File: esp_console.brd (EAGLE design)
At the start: 121.9 x 81.9 mm, 37 parts, among them IC1 74AHC1G04DBV, IC2 UA78M05DCY, J2 10118193-0001LF, Q1 12mhz, Q2 ON_SEMICONDUCTOR_BC849BLT1GON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, Q3 ON_SEMICONDUCTOR_BC849BLT1GON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, SW1 OS102011MA1Q

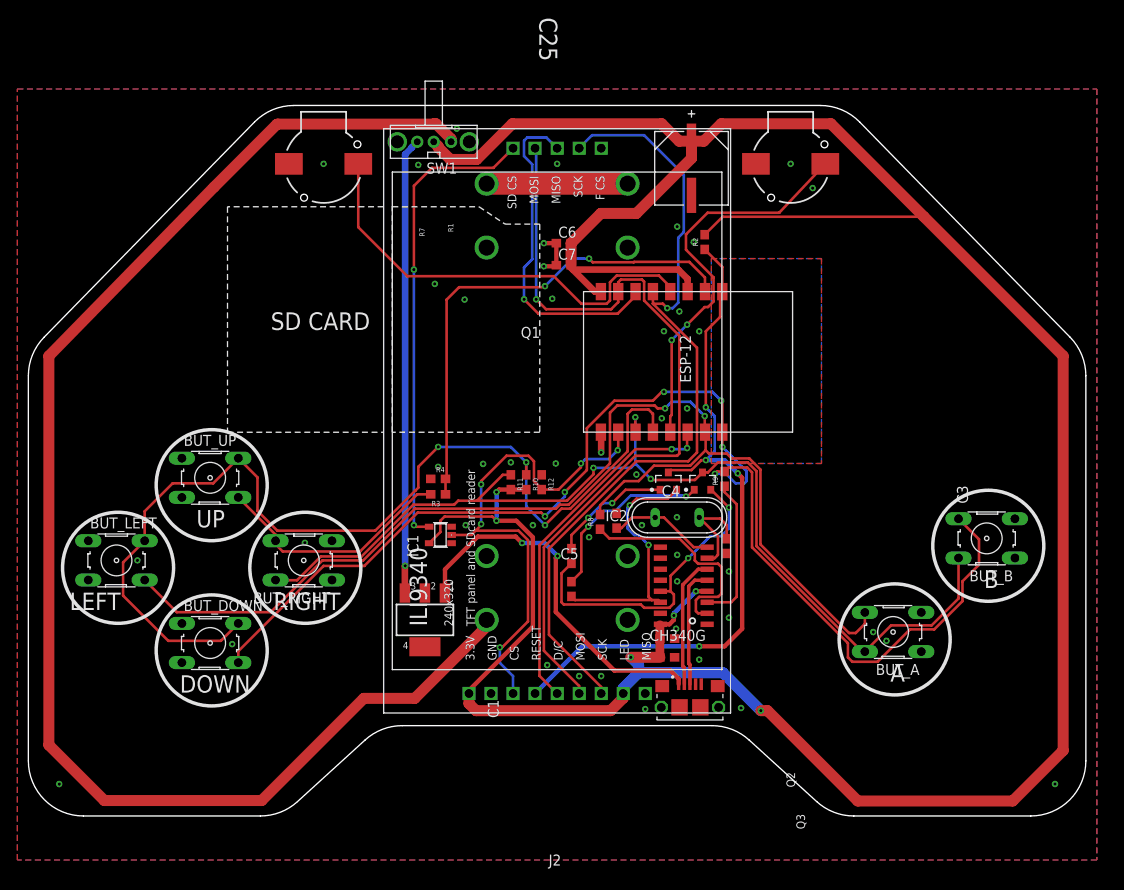
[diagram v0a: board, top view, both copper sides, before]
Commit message: Updated design to 8 buttons
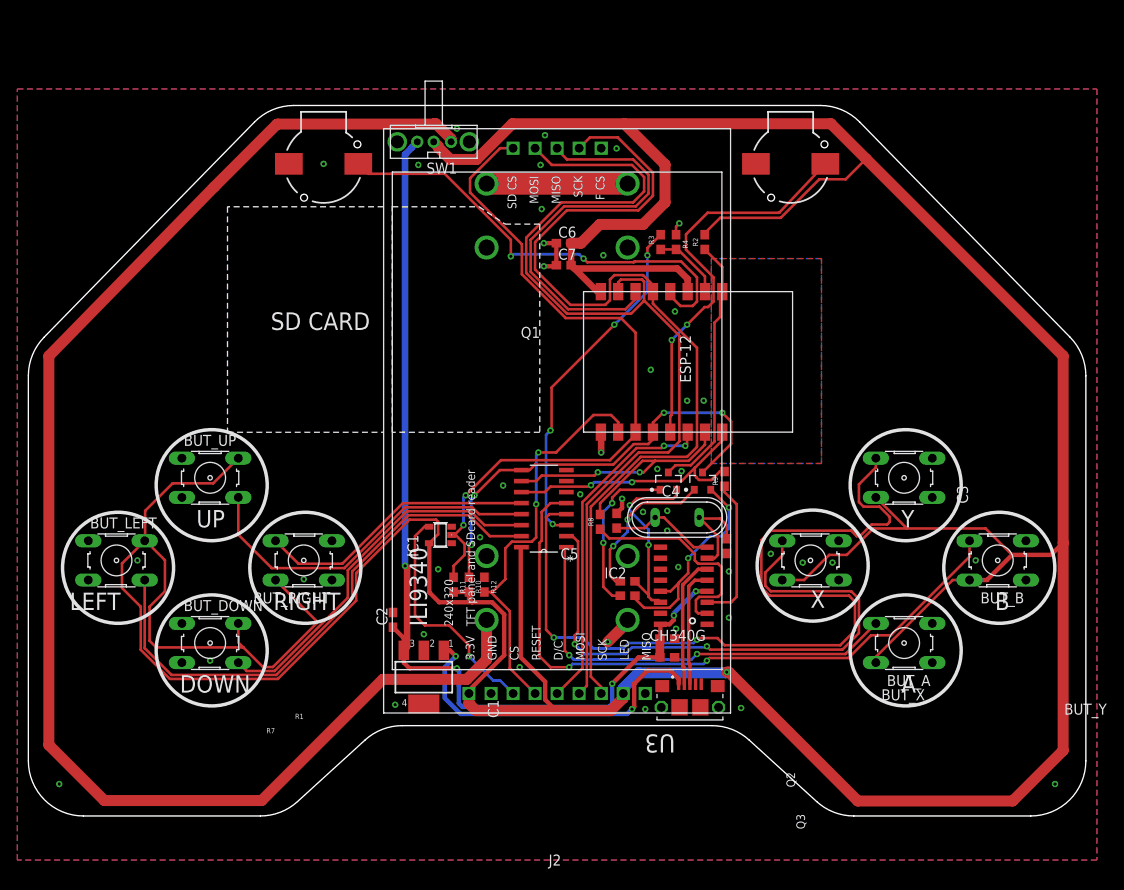
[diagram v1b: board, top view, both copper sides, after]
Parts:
- removed C25: 47uF, Panasonic-EEEFK_EEEFP:CAPAE830X1050N
- added BUT_X, BUT_Y: 0ohms, switch-omron:B3F-10XX
- added C2: 1uF, rcl:C0603
- added U3: 74HC4051D, 74HC4051D:SOIC127P600X175-16N
- moved R3 38.8 mm to (72.9, 56.0), turned to 90 degrees
- moved R4 38.7 mm to (74.7, 56.0), turned to 270 degrees
- moved R10 13.5 mm to (50.8, 16.5)
- moved R11 13.5 mm to (49.0, 16.5)
- moved R12 13.5 mm to (52.6, 16.5)
- moved R1 7.93 mm to (69.1, 15.2), turned to 0 degrees
- moved IC2 6.61 mm to (45.6, 5.84)
- moved R7 6.54 mm to (69.1, 16.9), turned to 0 degrees
- moved BUT_B 2.84 mm to (111.8, 19.3)
- moved BUT_A 1.80 mm to (101.0, 9.78)
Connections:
- net BUT_0 renamed BUT_READ
- removed net BUT_0_DIV: BUT_RIGHT.4, BUT_UP.4, R3.2
- removed net BUT_1: BUT_A.4, BUT_LEFT.4, MDL1.15, R8.2
- removed net BUT_2: BUT_B.4, BUT_DOWN.4, MDL1.16, R9.2
- removed net OUT_0: BUT_DOWN.2, BUT_LEFT.2, BUT_UP.2, MDL1.12, R10.1
- removed net OUT_1: BUT_A.2, BUT_B.2, BUT_RIGHT.2, MDL1.11, Q2.3, R11.1
- new net A: BUT_A.4, U3.1
- new net B: BUT_B.4, U3.5
- new net BUT_READ_3V3: R3.2, U3.3
- new net DOWN: BUT_DOWN.4, U3.14
- new net LEFT: BUT_LEFT.4, U3.15
- new net RIGHT: BUT_RIGHT.4, U3.12
- new net S0: MDL1.16, R9.2, U3.11
- new net S1: MDL1.15, R8.2, U3.10
- new net S2: MDL1.12, Q2.3, R10.1, U3.9
- new net TFT_RESET: MDL1.10, R12.2, U$2.TFT_RESET
- new net UP: BUT_UP.4, U3.13
- new net X: BUT_X.4, U3.2
- new net Y: BUT_Y.4, U3.4
- net CS_SIG: now also MDL1.11, R11.1, U$2.SD_CS; no longer MDL1.10, R12.2, U$2.TFT_CS
- net CS_SIG_INVERTED: now also U$2.TFT_CS; no longer U$2.SD_CS
- net GND: now also C2.2, U3.6, U3.7, U3.8; no longer C25.2
- net MCU_RESET: no longer U$2.TFT_RESET
- net REG_VCC: now also C2.1, C4.1, C5.1, U$1.16, U$1.4
- net VCC: now also BUT_A.2, BUT_B.2, BUT_DOWN.2, BUT_LEFT.2, BUT_RIGHT.2, BUT_UP.2, BUT_X.2, BUT_Y.2, U3.16; no longer C25.1, C4.1, C5.1, U$1.16, U$1.4
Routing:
- net VCC: track 342.7 -> 519.8 mm, vias 6 -> 1
- net BUT_2: track 146.3 -> 0.00 mm, vias 6 -> 0
- net BUT_1: track 134.3 -> 0.00 mm, vias 2 -> 0
- net OUT_1: track 119.9 -> 0.00 mm, vias 3 -> 0
- net OUT_0: track 117.8 -> 0.00 mm, vias 3 -> 0
- net Y: track 0.00 -> 100.7 mm, vias 0 -> 2
- net B: track 0.00 -> 77.2 mm, vias 0 -> 2
- net X: track 0.00 -> 69.5 mm, vias 0 -> 2
- net LEFT: track 0.00 -> 63.1 mm
- net REG_VCC: track 52.6 -> 112.9 mm, vias 1 -> 5
- net S2: track 0.00 -> 52.0 mm, vias 0 -> 4
- net MCU_RESET: track 81.1 -> 30.2 mm, vias 4 -> 0
- net A: track 0.00 -> 50.0 mm, vias 0 -> 2
- net BUT_READ: track 56.8 -> 8.15 mm, vias 2 -> 0
- net TFT_RESET: track 0.00 -> 46.9 mm, vias 0 -> 2
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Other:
- board text added: "X"
- board text added: "Y"

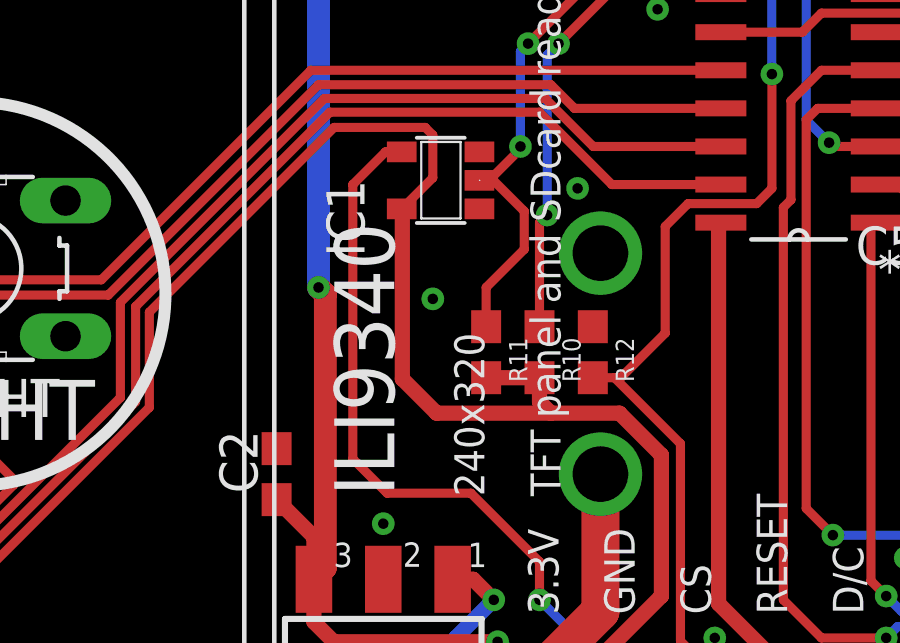
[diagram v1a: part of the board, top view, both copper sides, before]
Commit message: Added pullup to inverter, new gerbers
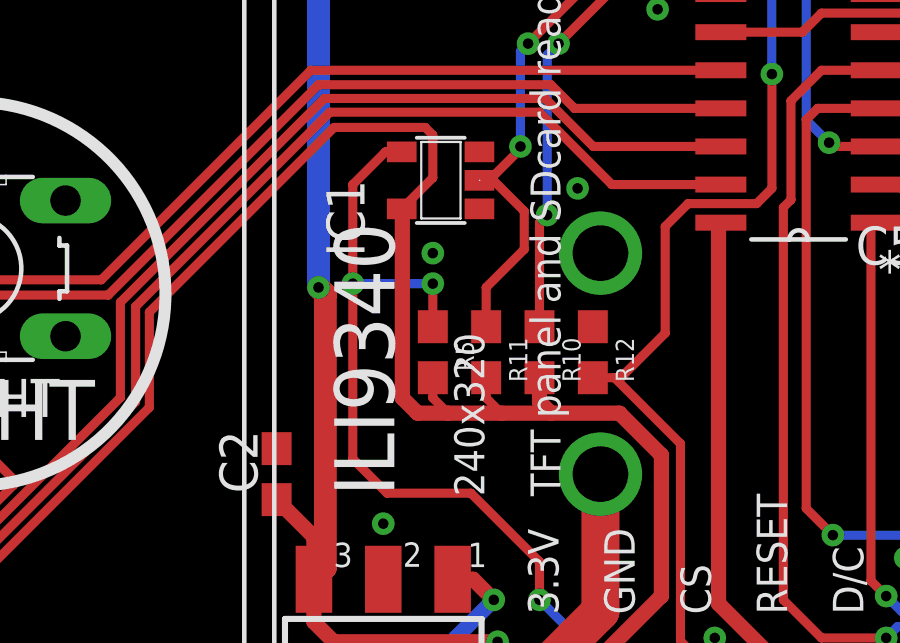
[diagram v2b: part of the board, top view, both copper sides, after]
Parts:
- added R5: 100k, SparkFun-Resistors:0603
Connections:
- net CS_SIG_INVERTED: now also R5.1
- net VCC: now also R5.2
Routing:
- net CS_SIG_INVERTED: track 27.0 -> 31.1 mm, vias 1 -> 3
- net VCC: track 519.8 -> 521.2 mm
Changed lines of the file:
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@@
 <attribute name="VALUE" x="43.942" y="11.811" size="1.27" layer="27" rot="R90"/>
+</element>
+<element name="R5" library="SparkFun-Resistors" library_urn="urn:adsk.eagle:library:532" package="0603" package3d_urn="urn:adsk.eagle:package:39650/1" value="100k" x="47.244" y="16.51" smashed="yes" rot="R270">
+<attribute name="NAME" x="48.006" y="16.383" size="0.6096" layer="25" font="vector" ratio="20" rot="R270" align="bottom-center"/>
+<attribute name="PROD_ID" value="RES-00824" x="47.244" y="16.383" size="1.778" layer="27" rot="R270" display="off"/>
+<attribute name="VALUE" x="46.482" y="16.383" size="0.6096" layer="27" font="vector" ratio="20" rot="R270" align="top-center"/>
 </element>
 </elements>
@@
 <wire x1="68.58" y1="4.572" x2="70.358" y2="6.35" width="1.27" layer="16"/>
 <wire x1="70.358" y1="6.35" x2="80.43899375" y2="6.35" width="1.27" layer="16"/>
-<wire x1="50.8" y1="15.66" x2="49.022" y2="15.66" width="0.508" layer="1"/>
 <wire x1="50.8" y1="4.318" x2="54.864" y2="8.382" width="0.508" layer="1"/>
 <wire x1="50.8" y1="4.318" x2="50.8" y2="3.9624" width="0.508" layer="1"/>
@@
 <wire x1="73.406" y1="60.579" x2="73.406" y2="64.94779375" width="1.27" layer="1"/>
 <wire x1="54.864" y1="8.382" x2="54.864" y2="13.081" width="0.508" layer="1"/>
-<wire x1="47.371" y1="14.478" x2="46.228" y2="15.621" width="0.508" layer="1"/>
-<wire x1="46.228" y1="15.621" x2="46.228" y2="21.268" width="0.508" layer="1"/>
+<wire x1="46.736" y1="14.478" x2="46.228" y2="14.986" width="0.508" layer="1"/>
+<wire x1="46.228" y1="14.986" x2="46.228" y2="21.268" width="0.508" layer="1"/>
 <wire x1="46.228" y1="21.268" x2="46.208" y2="21.288" width="0.508" layer="1"/>
 <wire x1="54.864" y1="13.081" x2="53.467" y2="14.478" width="0.508" layer="1"/>
 <wire x1="53.467" y1="14.478" x2="51.181" y2="14.478" width="0.508" layer="1"/>
-<wire x1="51.181" y1="14.478" x2="47.371" y2="14.478" width="0.508" layer="1"/>
+<wire x1="51.181" y1="14.478" x2="49.53" y2="14.478" width="0.508" layer="1"/>
+<wire x1="49.53" y1="14.478" x2="47.752" y2="14.478" width="0.508" layer="1"/>
+<wire x1="47.752" y1="14.478" x2="46.736" y2="14.478" width="0.508" layer="1"/>
 <wire x1="77.978" y1="56.857" x2="77.978" y2="57.023" width="0.3048" layer="1"/>
 <wire x1="77.978" y1="57.023" x2="79.756" y2="58.801" width="0.3048" layer="1"/>
@@
 <wire x1="62.572" y1="53.34" x2="65.62" y2="50.292" width="0.762" layer="1"/>
 <wire x1="65.62" y1="50.292" x2="66.008" y2="50.292" width="0.762" layer="1"/>
+<contactref element="R5" pad="2"/>
+<wire x1="47.244" y1="15.66" x2="47.244" y2="14.986" width="0.3048" layer="1"/>
+<wire x1="47.244" y1="14.986" x2="47.752" y2="14.478" width="0.3048" layer="1"/>
+<wire x1="49.022" y1="15.66" x2="49.022" y2="14.986" width="0.3048" layer="1"/>
+<wire x1="49.022" y1="14.986" x2="49.53" y2="14.478" width="0.3048" layer="1"/>
 </signal>
 <signal name="MCU_RESET">
@@
 <via x="54.737" y="27.94" extent="1-16" drill="0.35"/>
 <via x="52.07" y="21.971" extent="1-16" drill="0.35"/>
-<via x="47.244" y="18.288" extent="1-16" drill="0.35"/>
+<via x="47.244" y="19.812" extent="1-16" drill="0.35"/>
 <via x="63.627" y="26.924" extent="1-16" drill="0.35"/>
 <via x="68.453" y="26.416" extent="1-16" drill="0.35"/>
@@
 <wire x1="46.208" y1="23.188" x2="45.667" y2="23.188" width="0.3048" layer="1"/>
 <wire x1="45.667" y1="23.188" x2="44.577" y2="22.098" width="0.3048" layer="1"/>
-<wire x1="44.577" y1="22.098" x2="44.577" y2="12.954" width="0.3048" layer="1"/>
+<wire x1="44.577" y1="22.098" x2="44.577" y2="18.796" width="0.3048" layer="1"/>
+<wire x1="44.577" y1="18.796" x2="44.577" y2="12.954" width="0.3048" layer="1"/>
 <wire x1="45.72" y1="11.811" x2="48.514" y2="11.811" width="0.3048" layer="1"/>
 <wire x1="48.514" y1="11.811" x2="50.8" y2="9.525" width="0.3048" layer="1"/>
@@
 <wire x1="44.577" y1="12.954" x2="45.72" y2="11.811" width="0.3048" layer="1"/>
 <wire x1="53.594" y1="5.461" x2="54.3814" y2="5.461" width="0.3048" layer="16"/>
+<contactref element="R5" pad="1"/>
+<wire x1="47.244" y1="17.36" x2="47.244" y2="18.796" width="0.3048" layer="1"/>
+<via x="47.244" y="18.796" extent="1-16" drill="0.35"/>
+<wire x1="47.244" y1="18.796" x2="44.577" y2="18.796" width="0.3048" layer="16"/>
+<via x="44.577" y="18.796" extent="1-16" drill="0.35"/>
 </signal>
 <signal name="BUT_READ">

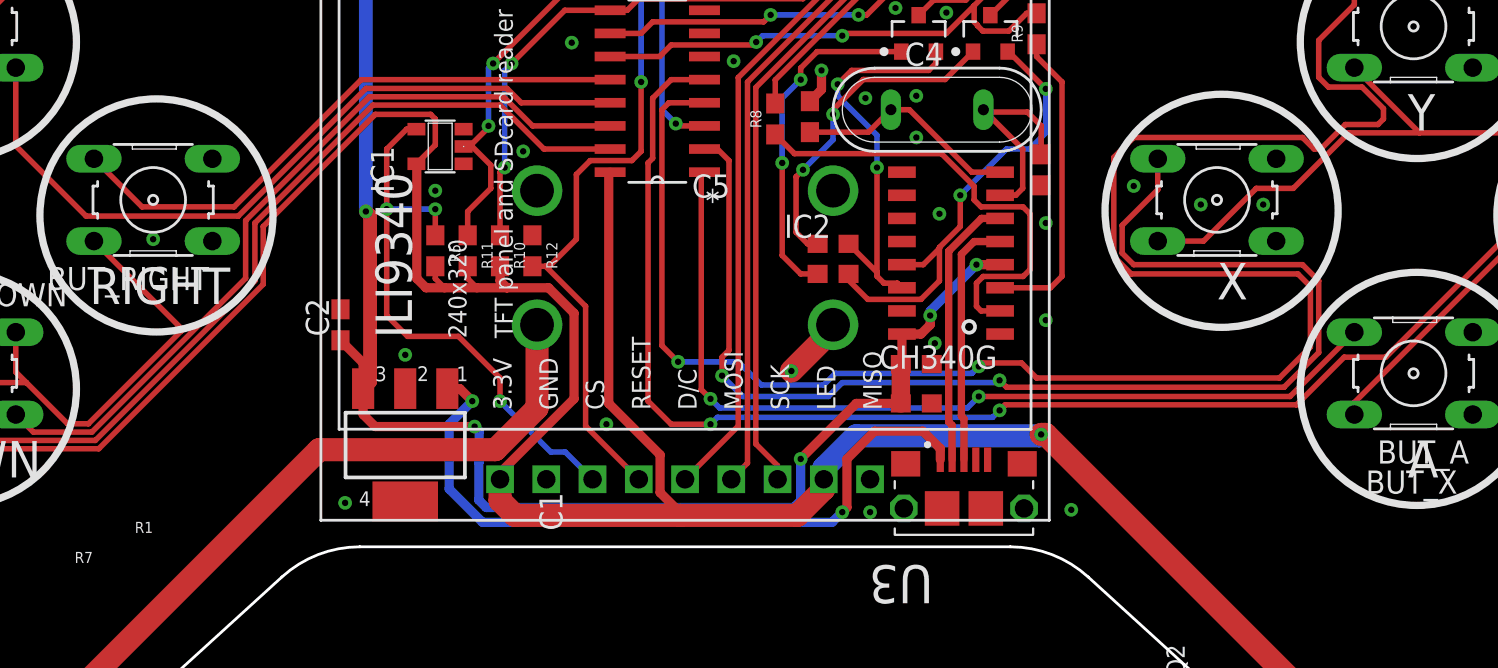
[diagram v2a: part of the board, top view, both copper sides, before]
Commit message: Slight revision to wire routing, new gerbers
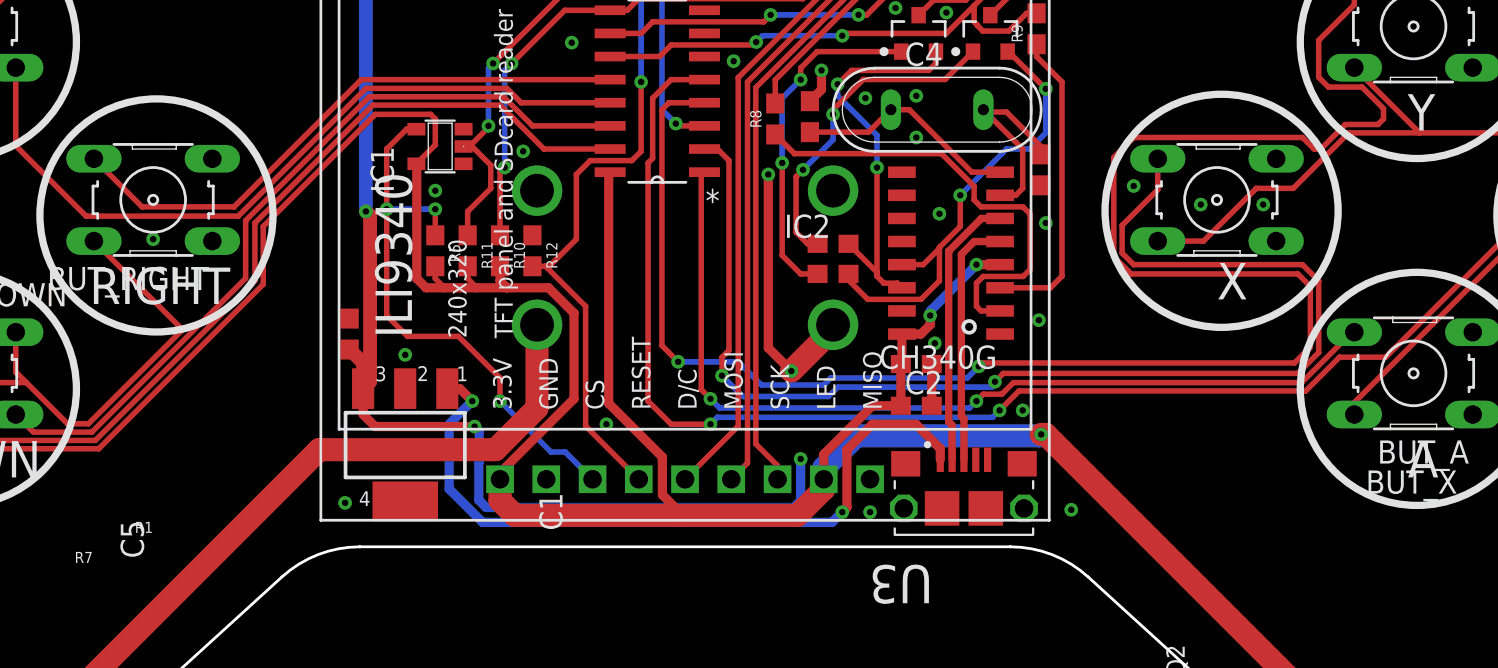
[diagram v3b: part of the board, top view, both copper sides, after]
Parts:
- moved C2 31.9 mm to (73.7, 8.00), turned to 0 degrees
- moved C5 31.3 mm to (42.5, 11.9), turned to 90 degrees
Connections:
- net REG_VCC: no longer C2.1, C4.1, U$1.16, U$1.4
- net VCC: now also C2.1, C4.1, U$1.16, U$1.4
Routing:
- net REG_VCC: track 112.9 -> 94.2 mm, vias 5 -> 3
- net VCC: track 521.2 -> 539.3 mm, vias 1 -> 3
- net GND: track 14.7 -> 28.4 mm, vias 45 -> 47
- net Y: track 100.7 -> 100.0 mm
- net CRYSTALIN: track 11.7 -> 11.0 mm
- net SUPPLY: track 39.4 -> 40.0 mm
